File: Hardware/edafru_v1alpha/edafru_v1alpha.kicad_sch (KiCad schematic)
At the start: 0 parts

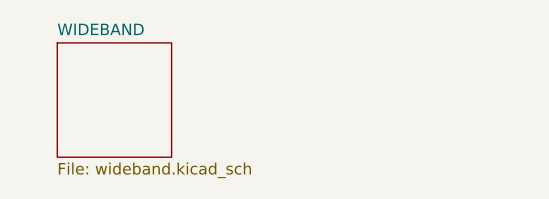
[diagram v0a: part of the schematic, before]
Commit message: all need circuits included to the schematic. ready for pcb component placement.
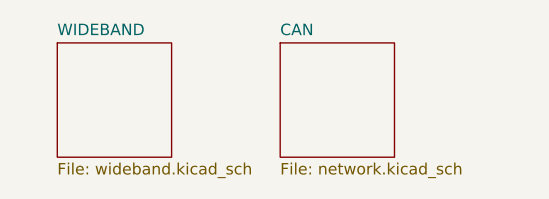
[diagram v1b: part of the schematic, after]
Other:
- added sheet CAN (network.kicad_sch)
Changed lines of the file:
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@@
+	)
+	(sheet
+		(at 151.765 63.5)
+		(size 12.7 12.7)
+		(exclude_from_sim no)
+		(in_bom yes)
+		(on_board yes)
+		(dnp no)
+		(fields_autoplaced yes)
+		(stroke
+			(width 0.1524)
+			(type solid)
+		)
+		(fill
+			(color 0 0 0 0)
+		)
+		(property "Sheetname" "CAN"
+			(at 151.765 62.7884 0)
+			(show_name no)
+			(do_not_autoplace no)
+			(effects
+				(font
+					(size 1.27 1.27)
+				)
+				(justify left bottom)
+			)
+		)
+		(property "Sheetfile" "network.kicad_sch"
+			(at 151.765 76.7846 0)
+			(show_name no)
+			(do_not_autoplace no)
+			(effects
+				(font
+					(size 1.27 1.27)
+				)
+				(justify left top)
+			)
+		)
+		(instances
+			(project "edafru_v1alpha"
+				(path "/1dc48840-f580-417d-a652-f8262e7cf75b"
+					(page "5")
+				)
+			)
+		)
 	)
 	(sheet

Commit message: PCB is developing...
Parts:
- added H1, H2, H3, H4: MountingHole_Pad_MP, MountingHole:MountingHole_3.2mm_M3_ISO14580_Pad, symbol Mechanical:MountingHole_Pad_MP
- added J1: Raspberry_Pi_4, Connector_PinSocket_2.54mm:PinSocket_2x20_P2.54mm_Vertical, symbol Connector:Raspberry_Pi_4
- added J2: DE9_Pins_MountingHoles, Connector_Dsub:DSUB-9_Pins_Horizontal_P2.77x2.84mm_EdgePinOffset4.94mm_Housed_MountingHolesOffset4.94mm, symbol Connector:DE9_Pins_MountingHoles
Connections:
- new net: J1.1 (3V3), J1.17 (3V3)
- new net +5V: J1.2 (5V), J1.4 (5V)
- new net +BATT: J2.9
- new net -BATT: J2.3
- new net BUS_SP1_MISO: J1.21 (MISO_SPI0/GPIO09)
- new net BUS_SPI1_MOSI: J1.19 (MOSI_SPI0/GPIO10)
- new net BUS_SPI1_SCK: J1.23 (SCLK_SPI0/GPIO11)
- new net CAN_H: J2.7
- new net CAN_L: J2.2
- new net COM_RX: J1.8 (GPIO14/UART_TXD)
- new net COM_TX: J1.10 (GPIO15/UART_RXD)
- new net EEPROM_SPI1_NSS: J1.26 (~{CE1}_SPI0/GPIO07)
- new net GND: H1.MP, H2.MP, H3.MP, H4.MP, J1.14 (GND), J1.20 (GND), J1.25 (GND), J1.30 (GND), J1.34 (GND), J1.39 (GND), J1.6 (GND), J1.9 (GND)
- new net LIN_BUS: J2.8
- new net LIN_INH: J2.4
- new net WIDEBAND_SPI1_NSS: J1.24 (~{CE0}_SPI0/GPIO08)
- no-connect marks 0 -> 22
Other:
- sheet CAN renamed NETWORK

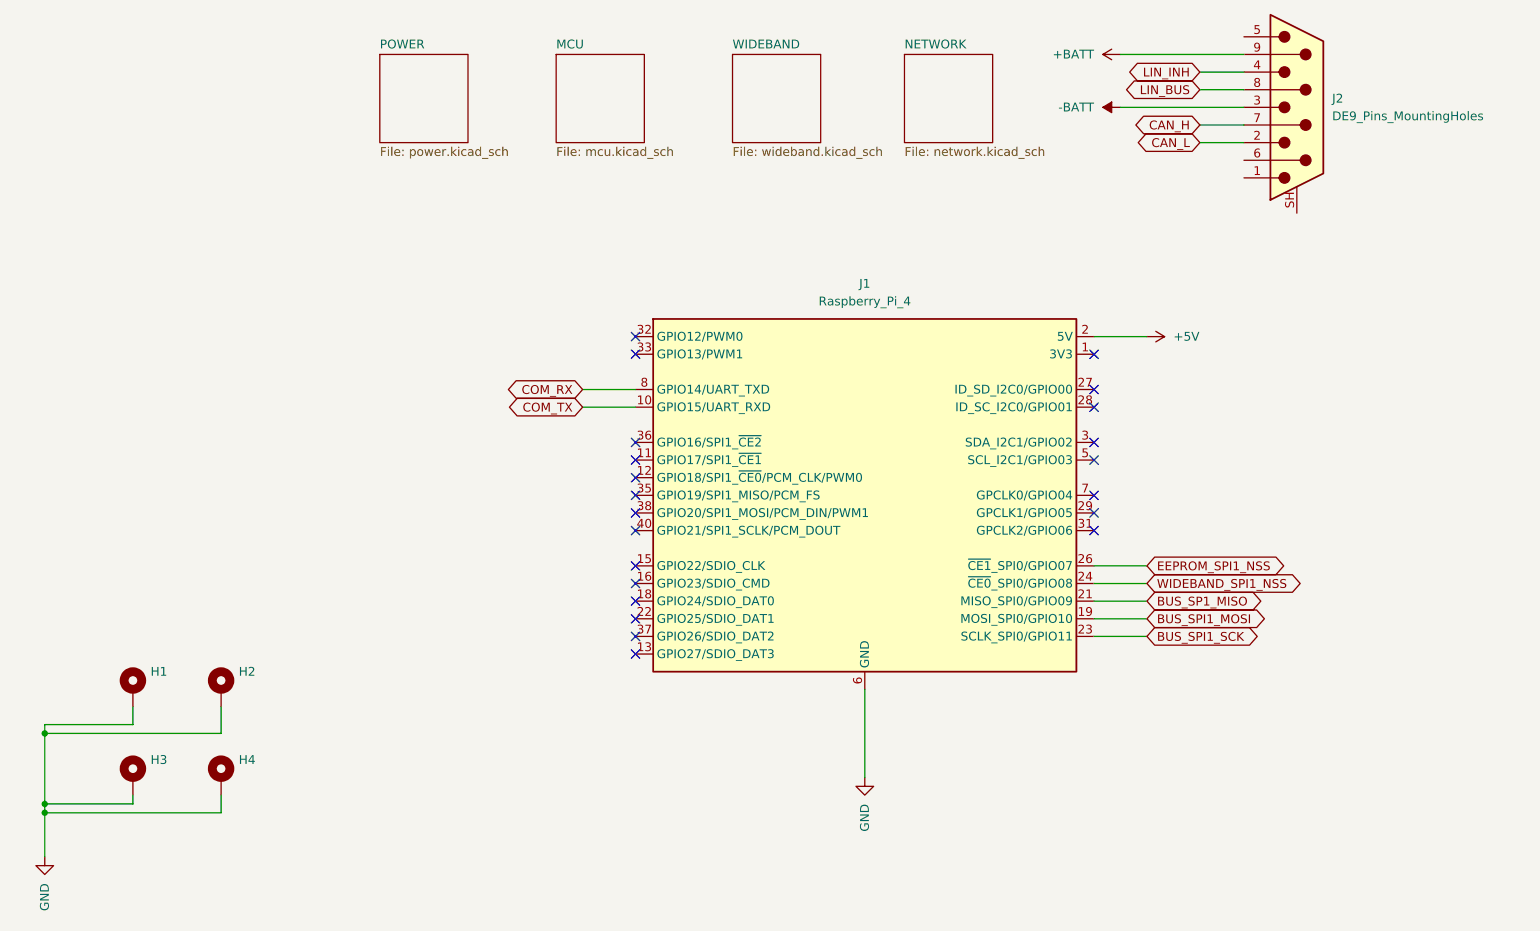
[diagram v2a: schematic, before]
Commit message: developement is stopped depend on new EDVDU.
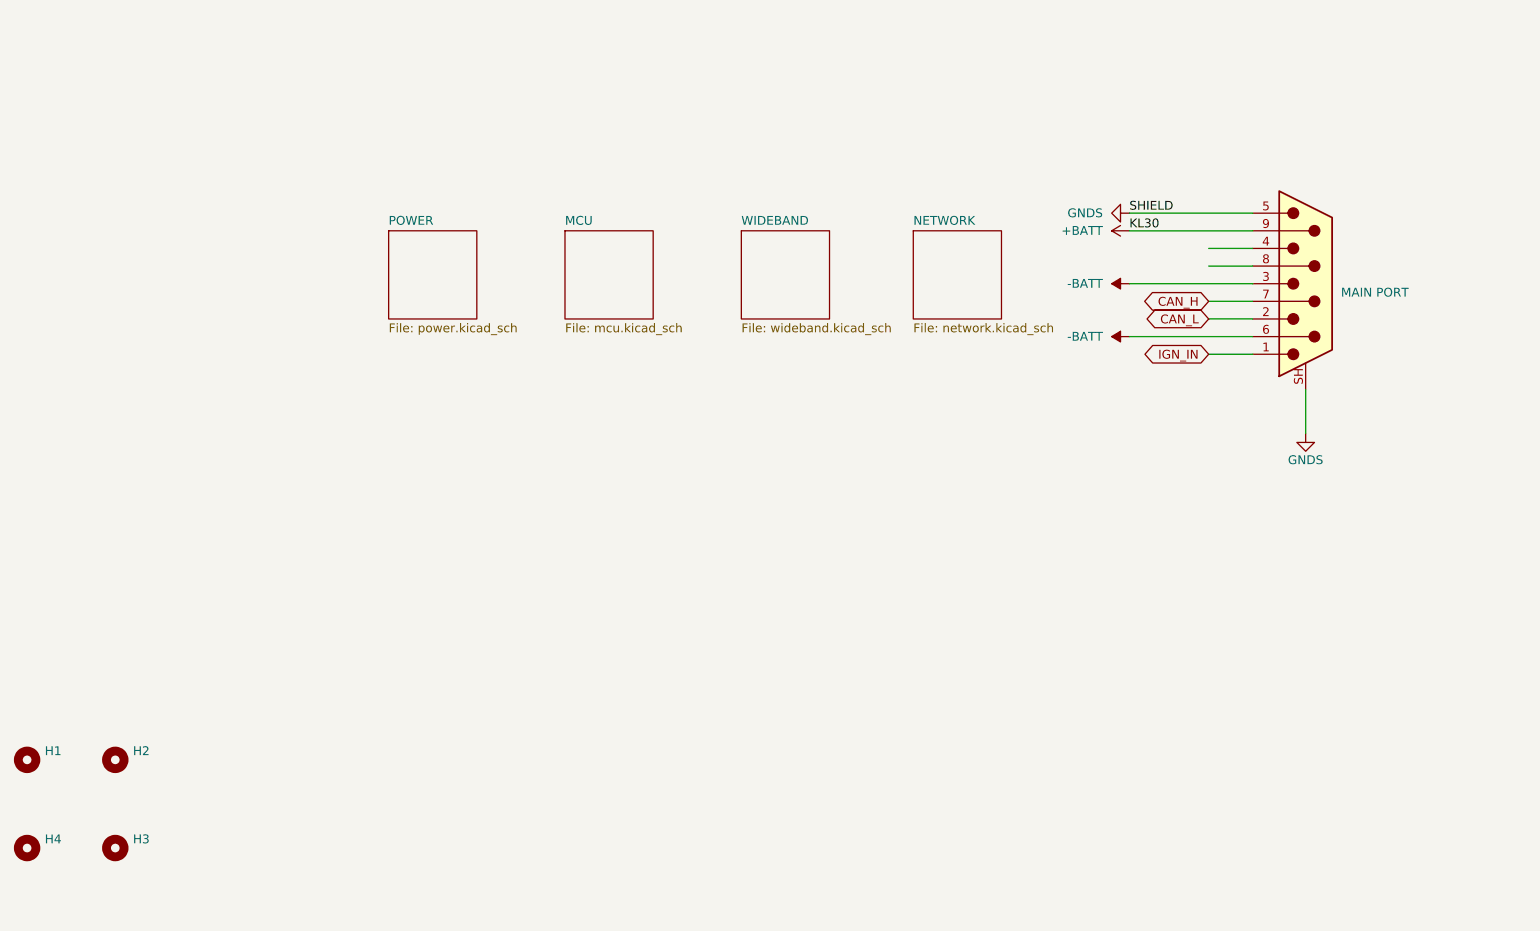
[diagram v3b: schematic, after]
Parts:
- removed H1, H2, H3, H4: MountingHole_Pad_MP, MountingHole:MountingHole_3.2mm_M3_ISO14580_Pad, symbol Mechanical:MountingHole_Pad_MP
- removed J1: Raspberry_Pi_4, Connector_PinSocket_2.54mm:PinSocket_2x20_P2.54mm_Vertical, symbol Connector:Raspberry_Pi_4
- added H1, H2, H3, H4: MountingHole, MountingHole:MountingHole_3.2mm_M3_DIN965, symbol Mechanical:MountingHole
- J2: value DE9_Pins_MountingHoles -> MAIN PORT
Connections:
- net -BATT: now also J2.6
- net IGN_IN: now reaches J2.1
- net GNDS: now reaches J2.5
- net GNDS: now also J2.SH (PAD)
- net LIN_BUS: no longer names the net of J2.8
- net LIN_INH: no longer names the net of J2.4
- no-connect marks 22 -> 0
